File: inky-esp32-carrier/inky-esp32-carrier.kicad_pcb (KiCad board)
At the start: 2 copper layers, 65 x 30 mm, 29 parts, among them J1 USB_C_Receptacle, J2 Inky_Impression_GPIO, J3 UART0, SW1 RESET, SW2 BOOT, U1 ESP32-S3-WROOM-1-N16R8, U2 SGM2212-3.3XKC3G/TR

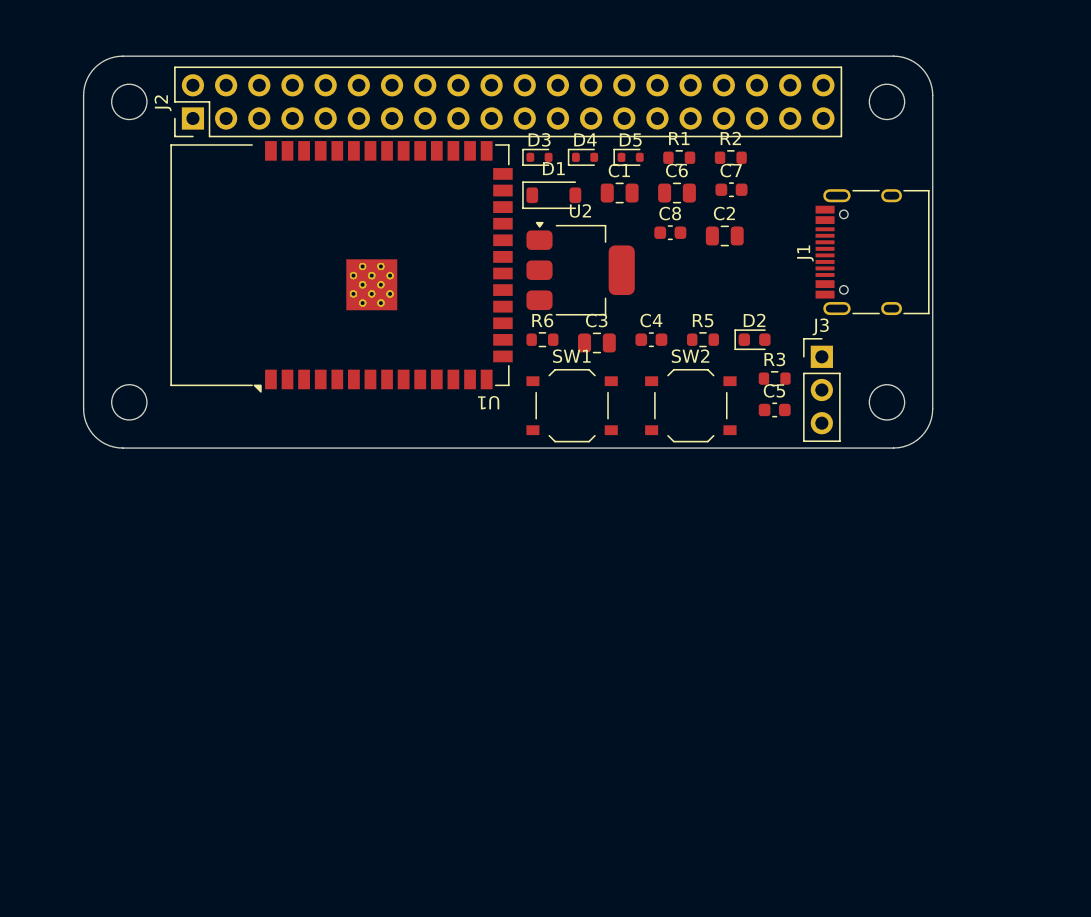
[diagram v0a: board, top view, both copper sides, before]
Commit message: Setup page: restart the frame after saving or drawing
Taking the serial port stops the frame's loop, so saving settings or drawing a
block left the frame idle until someone reset it by hand. Both now reset the
board when they finish.

Co-Authored-By: Claude Opus 5 <noreply@anthropic.com>
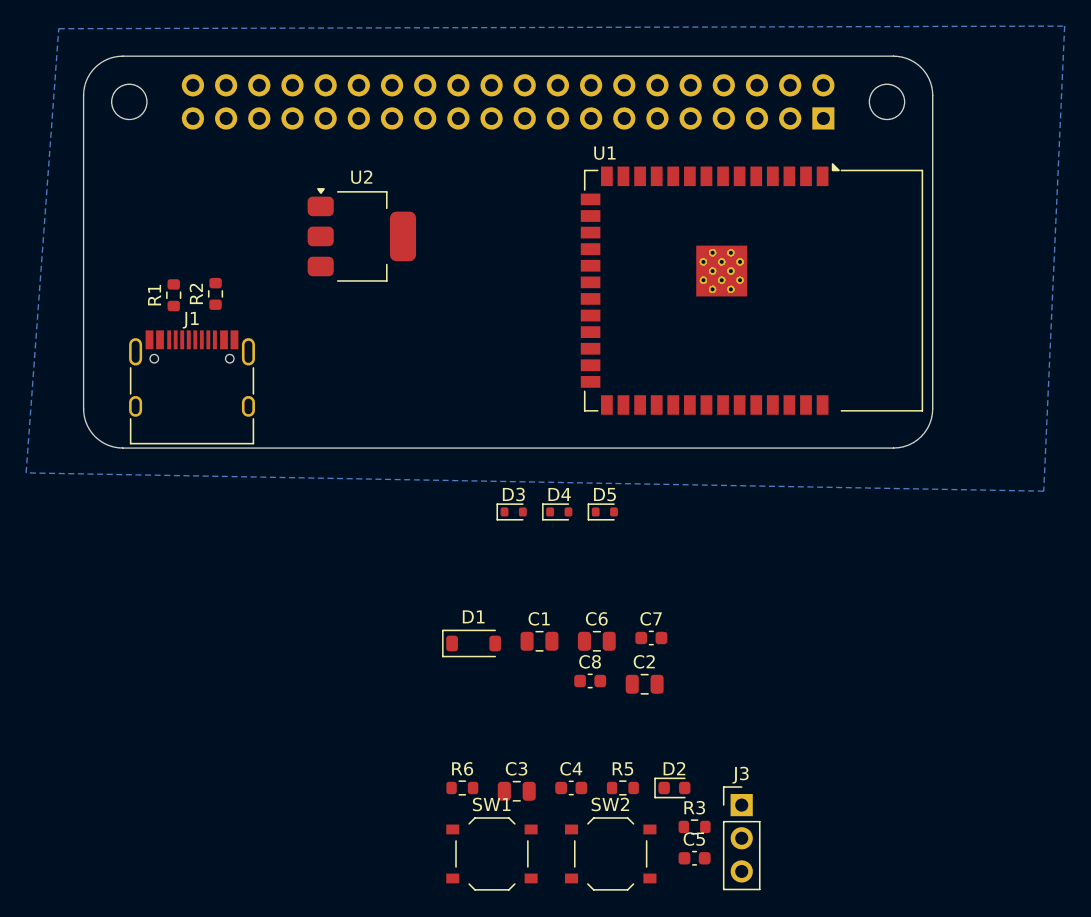
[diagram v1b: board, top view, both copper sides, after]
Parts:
- removed H3, H4: MountingHole_M2.5, MountingHole:MountingHole_2.7mm_M2.5
- J2: moved to B.Cu
- moved J1 53.6 mm to (108.3, 105.8), turned to 0 degrees
- moved J2 48.3 mm to (156.6, 84.8)
- moved R2 40.8 mm to (110.1, 98.2), turned to 90 degrees
- moved R1 40.1 mm to (106.9, 98.3), turned to 90 degrees
- moved C2 34.9 mm to (142.9, 128.1)
- moved C6 34.9 mm to (139.3, 124.8)
- moved D2 34.9 mm to (145.2, 136.0)
- moved C1 34.9 mm to (134.9, 124.8)
- moved C3 34.9 mm to (133.2, 136.3)
- moved C4 34.9 mm to (137.3, 136.0)
- moved C5 34.9 mm to (146.8, 141.4)
- moved C7 34.9 mm to (143.5, 124.5)
- moved J3 34.9 mm to (150.4, 137.3)
- moved R5 34.9 mm to (141.3, 136.0)
- moved R6 34.9 mm to (129.0, 136.0)
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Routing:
- added copper zone on B.Cu, net GND
